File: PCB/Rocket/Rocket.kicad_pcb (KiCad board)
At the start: 2 copper layers, 62.7 x 63.5 mm, 47 parts, among them J1 Conn_01x08_Pin, J2 Conn_01x04_Pin, J3 Conn_01x07_Pin, J4 Micro_SD_Card, J5 Conn_ARM_JTAG_SWD_10, J6 Conn_01x04_Pin, J7 1987724, SW1 CK_KMS2xxG, SW2 CK_KMS2xxG, U1 STM32L476RGTx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

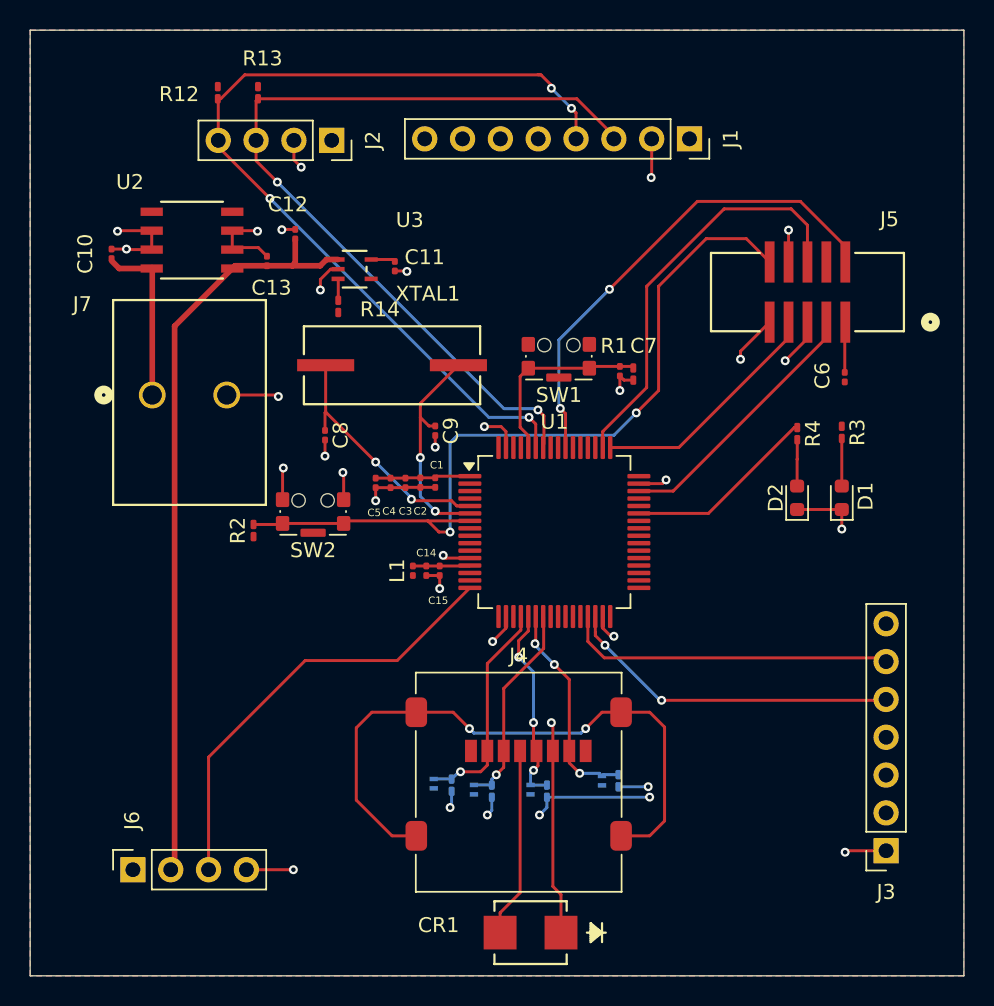
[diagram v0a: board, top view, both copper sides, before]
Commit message: Updated footprints for regulators and silkscreen.
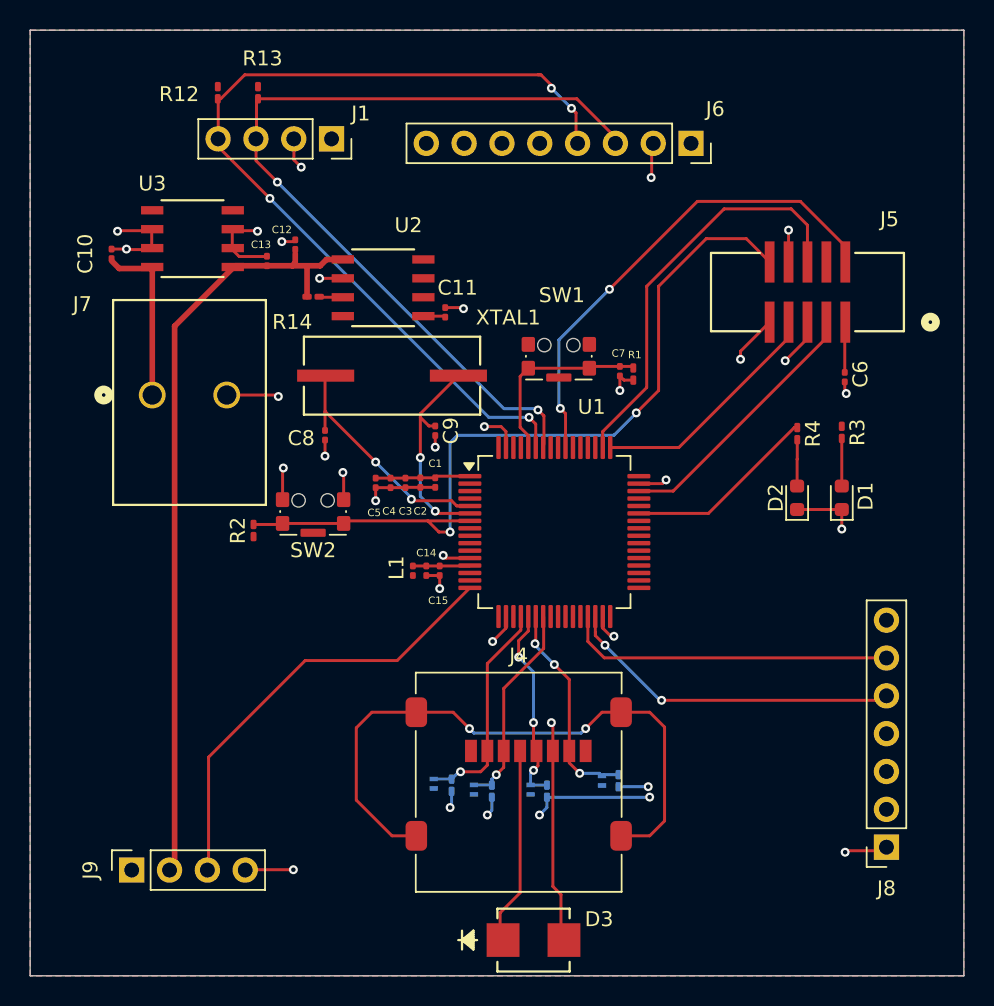
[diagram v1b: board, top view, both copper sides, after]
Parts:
- removed CR1: SMLVT3V3, SMLVT3V3:SMB_STM
- removed J2: Conn_01x04_Pin, Connector_PinSocket_2.54mm:PinSocket_1x04_P2.54mm_Vertical
- removed J3: Conn_01x07_Pin, Connector_PinSocket_2.54mm:PinSocket_1x07_P2.54mm_Vertical
- added D3: SMLVT3V3, SMLVT3V3:SMB_STM, F.Cu at (136.6, 97.9)
- added J8: ~, Connector_PinSocket_2.54mm:PinSocket_1x07_P2.54mm_Vertical, F.Cu at (160.3, 91.7)
- added J9: ~, Connector_PinSocket_2.54mm:PinSocket_1x04_P2.54mm_Vertical, F.Cu at (109.6, 93.2)
- J1: value Conn_01x08_Pin -> ~; footprint Connector_PinSocket_2.54mm:PinSocket_1x08_P2.54mm_Vertical -> Connector_PinSocket_2.54mm:PinSocket_1x04_P2.54mm_Vertical
- J6: value Conn_01x04_Pin -> ~; footprint Connector_PinSocket_2.54mm:PinSocket_1x04_P2.54mm_Vertical -> Connector_PinSocket_2.54mm:PinSocket_1x08_P2.54mm_Vertical
- U2: value MC78L05ACDR2G -> MIC5365-3.3YC5-TR
- U3: value MIC5365-3.3YC5-TR -> MC78L05ACDR2G; footprint MIC5365-3.3YC5-TR:SC-70_C5_MCH -> MC78L05ACDR2G:SOIC8_ONS
- moved J6 61.5 mm to (147.2, 44.4), turned to -90 degrees
- moved J1 24.0 mm to (123.0, 44.1)
- moved U2 13.2 mm to (126.5, 54.1), turned to 0 degrees
- moved U3 11.1 mm to (113.7, 50.8), turned to 180 degrees
- moved C11 4.59 mm to (130.7, 55.8), turned to -90 degrees
- moved R14 1.81 mm to (121.8, 54.7), turned to 180 degrees
- moved C12 0.70 mm to (120.6, 51.2)
- moved XTAL1 0.70 mm to (127.1, 60.0)
- turned C6 to -90 degrees
- renumbered CR2 to D4, CR3 to D5, CR4 to D6, CR5 to D7
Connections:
- C6 pad 2: Net-(J5-VTref) -> GND
- J5 pad 1: Net-(J5-VTref) -> +3.3V
- J6 pad 1: unconnected-(J6-Pin_1-Pad1) -> +3.3V
- J6 pad 2: +5V -> GND
- J6 pad 3: /PRESSURE_OUT -> /SCL
- J6 pad 4: GND -> /SDA
- R14 pad 1: Net-(U3-EN) -> Net-(U2-EN)
- R14 pad 2: +3.3V -> +5V
- U2 pad 3: GND -> Net-(U2-EN)
- U2 pad 5: unconnected-(U2-NC-Pad5) -> +3.3V
- U2 pad 6: GND -> (no net)
- U2 pad 7: GND -> (no net)
- U2 pad 8: +VDC -> (no net)
- U3 pad 3: Net-(U3-EN) -> GND
- U3 pad 5: +3.3V -> unconnected-(U3-NC-Pad5)
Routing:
- net Net-(J5-VTref): track 3.39 -> 0.00 mm
- net +3.3V: track 33.8 -> 37.1 mm
- net Net-(U2-EN): track 0.00 -> 1.60 mm
- net Net-(U3-EN): track 1.45 -> 0.00 mm
- net +5V: track 51.3 -> 52.4 mm
- net /TX: track 22.9 -> 21.9 mm
- net /OSC_OUT: track 14.9 -> 14.2 mm
- net /OSC_IN: track 16.9 -> 16.2 mm
- net GND: track 82.1 -> 82.6 mm, vias 28 -> 29
